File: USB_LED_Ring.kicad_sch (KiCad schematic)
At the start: 69 parts, among them J1 .100, J2 USB_B_Micro, J3 JST SH 3 Vert, J4 JST SH 3 Vert, U1 TPS22917DBV, U2 TPS923610, U3 W25Q16JVUXIQ, U4 TLV75733PDBV, U5 RP2040, Y1 ABM8-272-T3

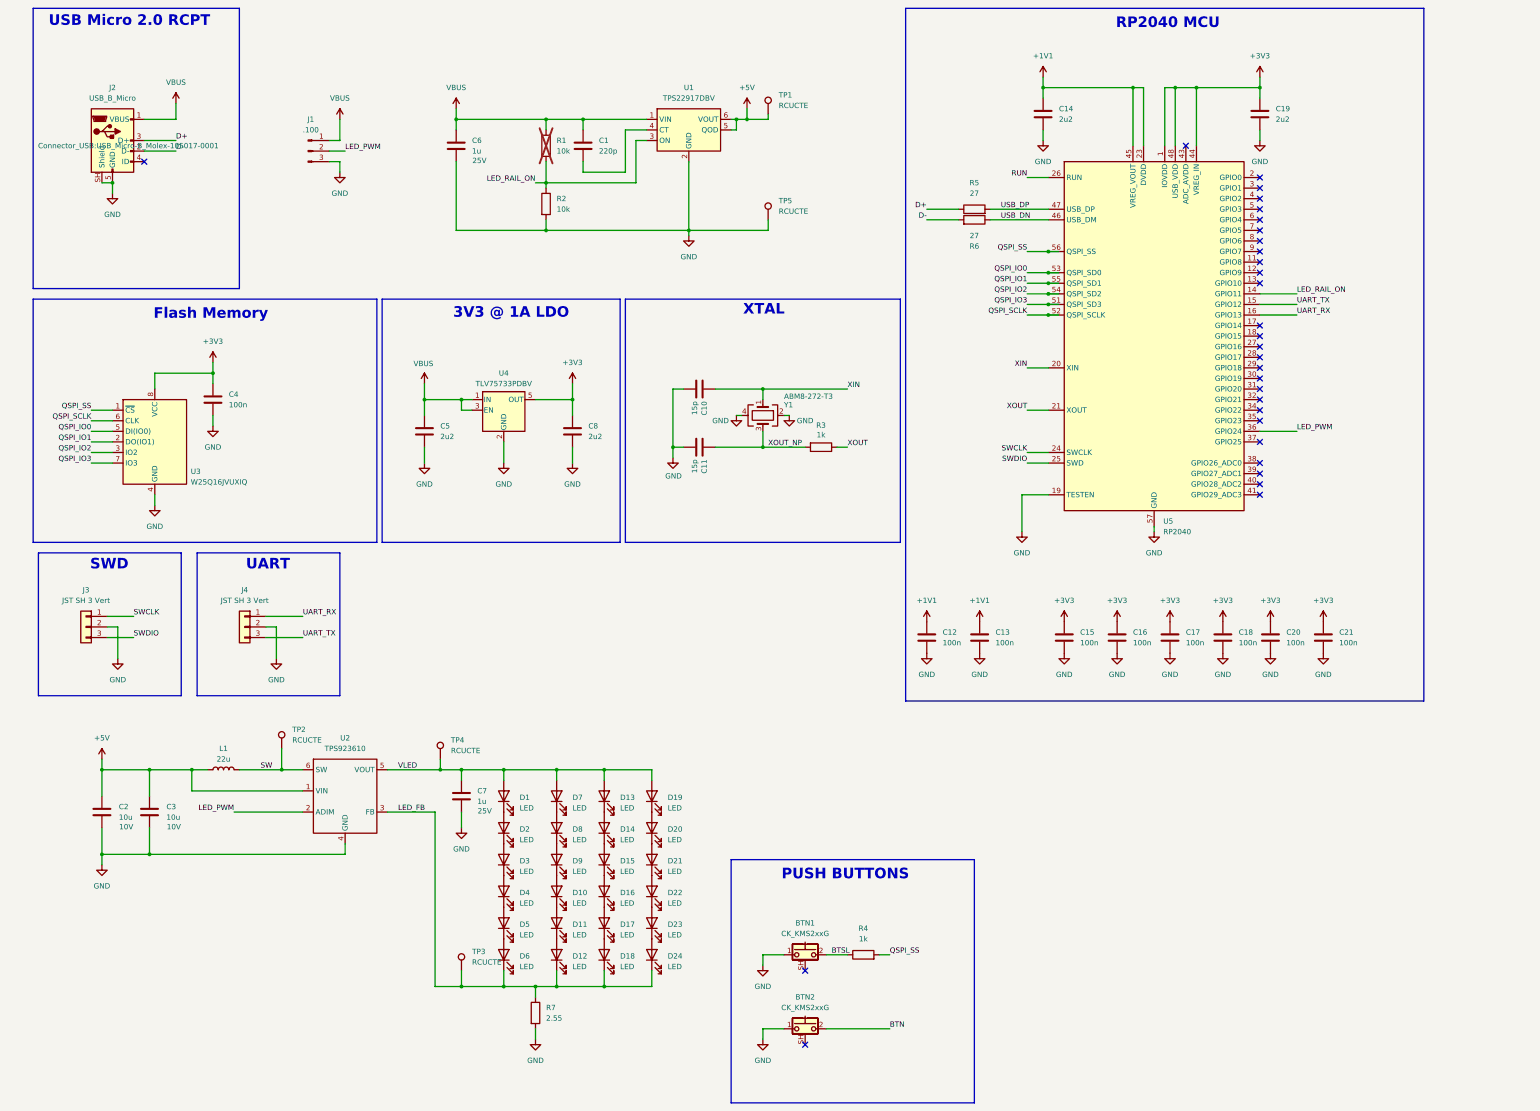
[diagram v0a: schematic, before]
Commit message: Uses RP2354A instead of RP2040 It simplifies the BOM a lot, and removes an hard to solder component
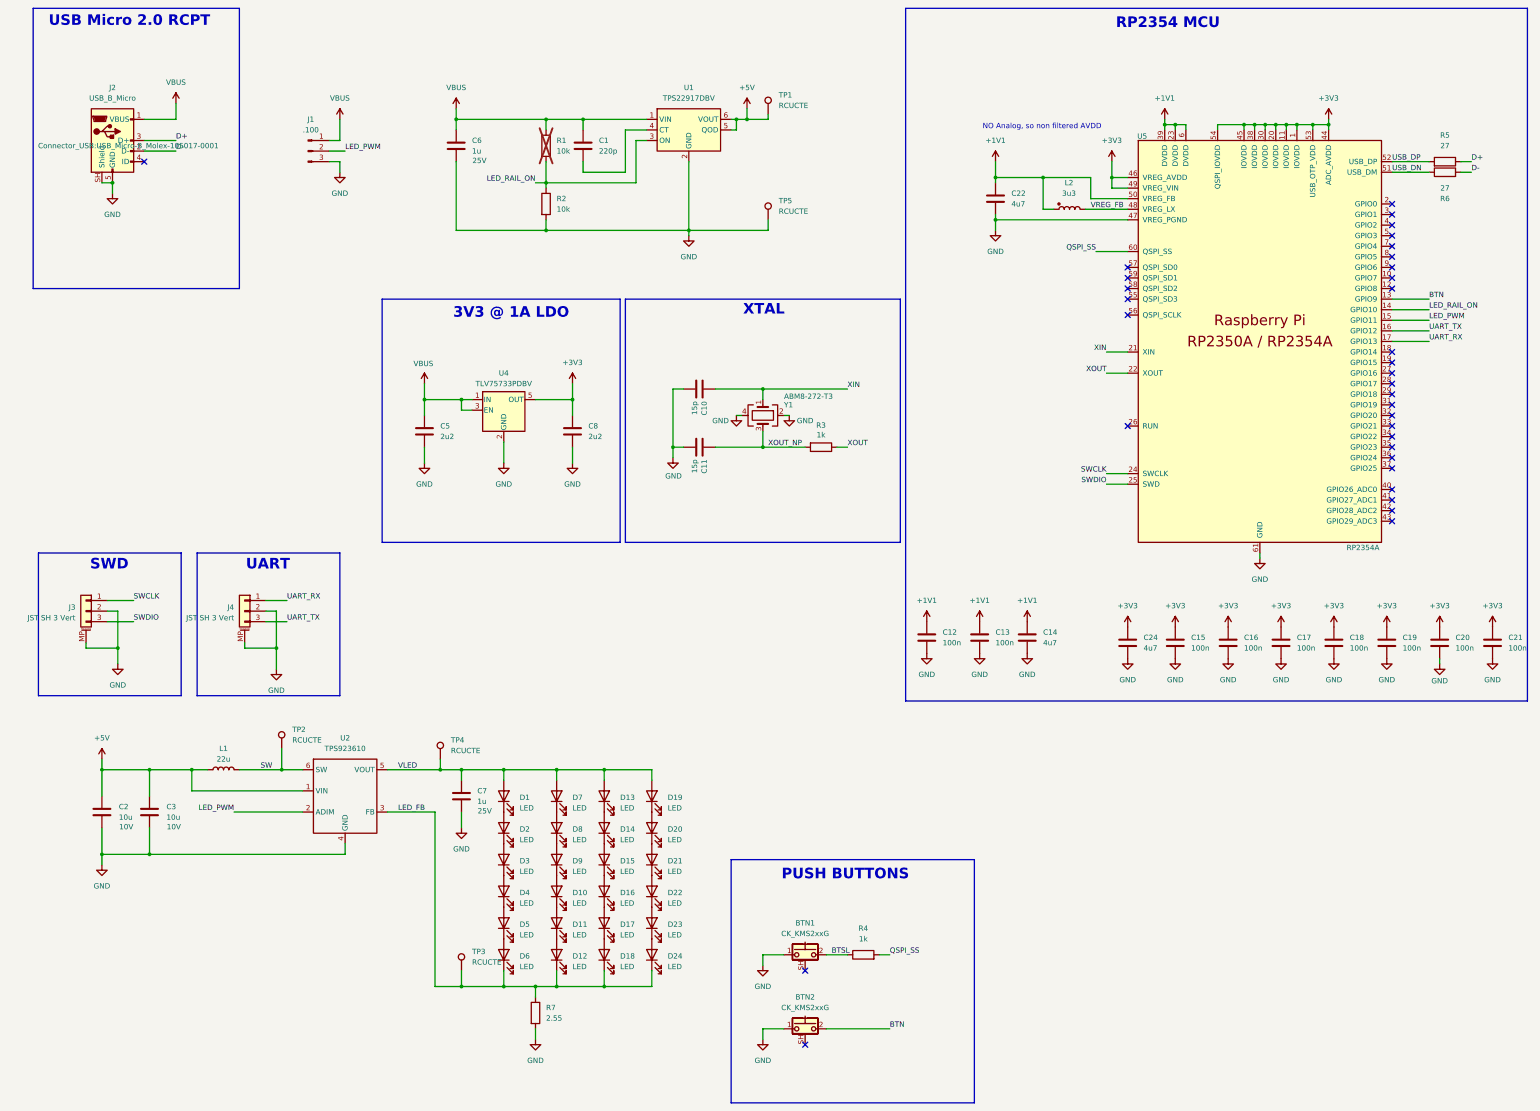
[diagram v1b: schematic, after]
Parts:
- removed C4: 100n, Capacitor_SMD:C_0402_1005Metric, symbol Device:C
- removed J3, J4: JST SH 3 Vert, Connector_JST:JST_SH_BM03B-SRSS-TB_1x03-1MP_P1.00mm_Vertical, symbol Connector_Generic:Conn_01x03
- removed U3: W25Q16JVUXIQ, Package_SON:Winbond_USON-8-1EP_3x2mm_P0.5mm_EP0.2x1.6mm, symbol Memory_Flash:W25Q16JVSS
- removed U5: RP2040, Package_DFN_QFN:QFN-56-1EP_7x7mm_P0.4mm_EP3.2x3.2mm, symbol MCU_RaspberryPi:RP2040
- added C22, C24: 4u7, Capacitor_SMD:C_0603_1608Metric, symbol Device:C
- added J3, J4: JST SH 3 Vert, Connector_JST:JST_SH_BM03B-SRSS-TB_1x03-1MP_P1.00mm_Vertical, symbol Connector_Generic_MountingPin:Conn_01x03_MountingPin
- added L2: 3u3, custom:L_Abracon_AOTA, symbol custom:L_Pol
- added U5: RP2354A, custom:RP2350-QFN-60-1EP_7x7_P0.4mm_EP3.4x3.4mm_ThermalVias, symbol custom:RP2354A
- C14: value 2u2 -> 4u7; footprint Capacitor_SMD:C_0402_1005Metric -> Capacitor_SMD:C_0603_1608Metric
- C19: value 2u2 -> 100n; MPN GRM155Z71A225KE01D -> CL05B104KP5NNNC
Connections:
- net +1V1: now also C22.1, L2.1, U5.23 (DVDD), U5.39 (DVDD), U5.50 (VREG_FB), U5.6 (DVDD)
- net +3V3: now also C24.1, U5.1 (IOVDD), U5.11 (IOVDD), U5.20 (IOVDD), U5.30 (IOVDD), U5.38 (IOVDD), U5.44 (ADC_AVDD), U5.45 (IOVDD), U5.46 (VREG_AVDD), U5.49 (VREG_VIN), U5.53 (USB_OTP_VDD), U5.54 (QSPI_IOVDD)
- net BTN: now also U5.13 (GPIO9)
- net GND: now also C22.2, C24.2, J3.2 (Pin_2), J3.MP (MountPin), J4.2 (Pin_2), J4.MP (MountPin), U5.47 (VREG_PGND), U5.61 (GND)
- net LED_PWM: now also U5.15 (GPIO11)
- net LED_RAIL_ON: now also U5.14 (GPIO10)
- net QSPI_SS: now also U5.60 (QSPI_SS)
- net SWCLK: now also J3.1 (Pin_1), U5.24 (SWCLK)
- net SWDIO: now also J3.3 (Pin_3), U5.25 (SWD)
- net UART_RX: now also J4.1 (Pin_1), U5.17 (GPIO13)
- net UART_TX: now also J4.3 (Pin_3), U5.16 (GPIO12)
- net USB_DN: now also U5.51 (USB_DM)
- net USB_DP: now also U5.52 (USB_DP)
- net XIN: now also U5.21 (XIN)
- net XOUT: now also U5.22 (XOUT)
- new net VREG_FB: L2.2, U5.48 (VREG_LX)
- no-connect marks 30 -> 34
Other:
- note added: "NO Analog, so non filtered AVDD"
- note added: "RP2354 MCU"
- note removed: "Flash Memory"
- note removed: "RP2040 MCU"
- moved on the sheet: C14, C15, C16, C17, C18, C20, C21, R5, R6

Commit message: Uses a Ferrite bead for Power Line Filtering.
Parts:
- removed C1: 220p, Capacitor_SMD:C_0603_1608Metric, symbol Device:C
- removed C3: 10u, Capacitor_SMD:C_0603_1608Metric, symbol Device:C
- removed C6: 1u, Capacitor_SMD:C_0603_1608Metric, symbol Device:C
- removed R1: 10k, Resistor_SMD:R_0603_1608Metric, symbol Device:R
- removed TP1: RCUCTE, custom:RCUCTE, symbol Connector:TestPoint
- removed U1: TPS22917DBV, Package_TO_SOT_SMD:SOT-23-6, symbol Power_Management:TPS22917DBV
- added C2: 100n, Capacitor_SMD:C_0402_1005Metric, symbol Device:C
- added FB1: MPZ1608S601A, Inductor_SMD:L_0603_1608Metric, symbol Device:FerriteBead
- added Q1: DMG2305UX, Package_TO_SOT_SMD:SOT-23, symbol Transistor_FET:Q_PMOS_GSD
- added TP4, TP6, TP7: RCUCTE, custom:RCUCTE, symbol Connector:TestPoint
- C1: renamed from C2; value 10u -> 4u7
- R2: value 10k -> 250m
- TP1: renamed from TP2; now not fitted
- TP2: renamed from TP4; now not fitted
- TP3, TP5: now not fitted
- renumbered C22 to C10, C14 to C11, C24 to C12, C15 to C13, C16 to C14, C17 to C15, C18 to C16, C19 to C17, C20 to C18, C21 to C19, C5 to C3, C7 to C4, C8 to C5, C10 to C6, C11 to C7, C12 to C8, C13 to C9, J3 to J1, J4 to J3, J1 to J4, R7 to R1, U2 to U1, U4 to U2, U5 to U3
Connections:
- net +5V: now also C2.1, FB1.1, TP7.1
- net GND: now also C2.2, Q1.1 (G), TP6.1; no longer R2.2, TP5.1
- net LED_PWM: now also U3.35 (GPIO23); no longer U3.15 (GPIO11)
- net VBUS: now also Q1.3 (D)
- net LED_RAIL_ON: no longer names the net of U3.14 (GPIO10)
- net LED_RAIL_ON: no longer R2.1
- new net: FB1.2, R2.2, TP5.1
- new net: Q1.2 (S), R2.1, TP4.1
- no-connect marks 34 -> 35
